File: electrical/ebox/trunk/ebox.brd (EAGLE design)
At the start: 127 x 101.6 mm, 161 parts, among them IC1 MAX3221CUE, IC10 SN74LVC1G125, IC11 MAX3221CUE, IC12 INA170, IC13 SN74LVC1G125, IC14 SN74LVC1G125, IC15 MAX3221CUE, IC16 MCP170333MB, IC17 SN74LVC1G125, IC18 SN74LVC1G125, IC19 74ALS04D, IC2 LT3652, IC3 XMEGA128A1, IC4 LT1161, IC5 SN74LVC1G125, IC6 SN74LVC1G125, IC7 MAX3221CUE, IC8 INA170, IC9 SN74LVC1G125, Q1 FDD4141TO252, U1 BLUETOOTH-RN42, U2 D2523T_, X1 7381-3PG-300, X10 DEANS-MALE, X11 B4B-ZR, X12 DEANS-MALE, X13 B4B-ZR, X14 22-23-2021, X15 DEANS-FEMALE, X16 DEANS-FEMALE, X17 USB_A, X18 22-23-2021, X2 7381-3PG-300, X3 7381-2PG-300, X4 17984-7PG-300, X5 17984-7PG-300, X6 17984-7PG-300, X7 17984-7PG-300, X8 22-23-2031, X9 22-23-2031

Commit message: Cleaned up more stuff.  Just need to do final check and silkscreen work.
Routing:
- net MOT1_C: track 30.6 -> 0.00 mm
- net MOT2_C: track 30.6 -> 0.00 mm
- net CHARGE: track 20.9 -> 0.00 mm
- net MOT2_A: track 20.0 -> 0.00 mm
- net MOT1_A: track 20.0 -> 0.00 mm
- net MOT2_B: track 18.5 -> 0.00 mm
- net MOT1_B: track 18.5 -> 0.00 mm
- net +3V3: track 424.1 -> 417.6 mm
- net BT_STATUS: track 64.8 -> 63.0 mm
- net N$19: track 60.2 -> 58.7 mm
- net N$7: track 28.9 -> 30.2 mm
- net N$14: track 60.2 -> 59.1 mm
- net N$20: track 80.5 -> 81.5 mm
- net N$16: track 97.5 -> 98.5 mm
- net N$15: track 74.5 -> 75.6 mm
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- added copper zone on layer 1, net CHARGE
- added copper zone on layer 1, net MOT1_A
- added copper zone on layer 1, net MOT1_B
- added copper zone on layer 1, net MOT1_C
- added copper zone on layer 1, net MOT2_A
- added copper zone on layer 1, net MOT2_B
- added copper zone on layer 1, net MOT2_C

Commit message: Updated some silkscreen on various areas.
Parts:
- moved X8 1.91 mm to (28.6, 5.08)
- moved X9 1.27 mm to (21.6, 5.08)
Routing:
- net MOT1_SIG: track 27.3 -> 29.2 mm
- net MOT1_5V: track 6.13 -> 8.04 mm
- net MOT2_5V: track 13.8 -> 15.0 mm
- net MOT2_SIG: track 35.4 -> 36.7 mm

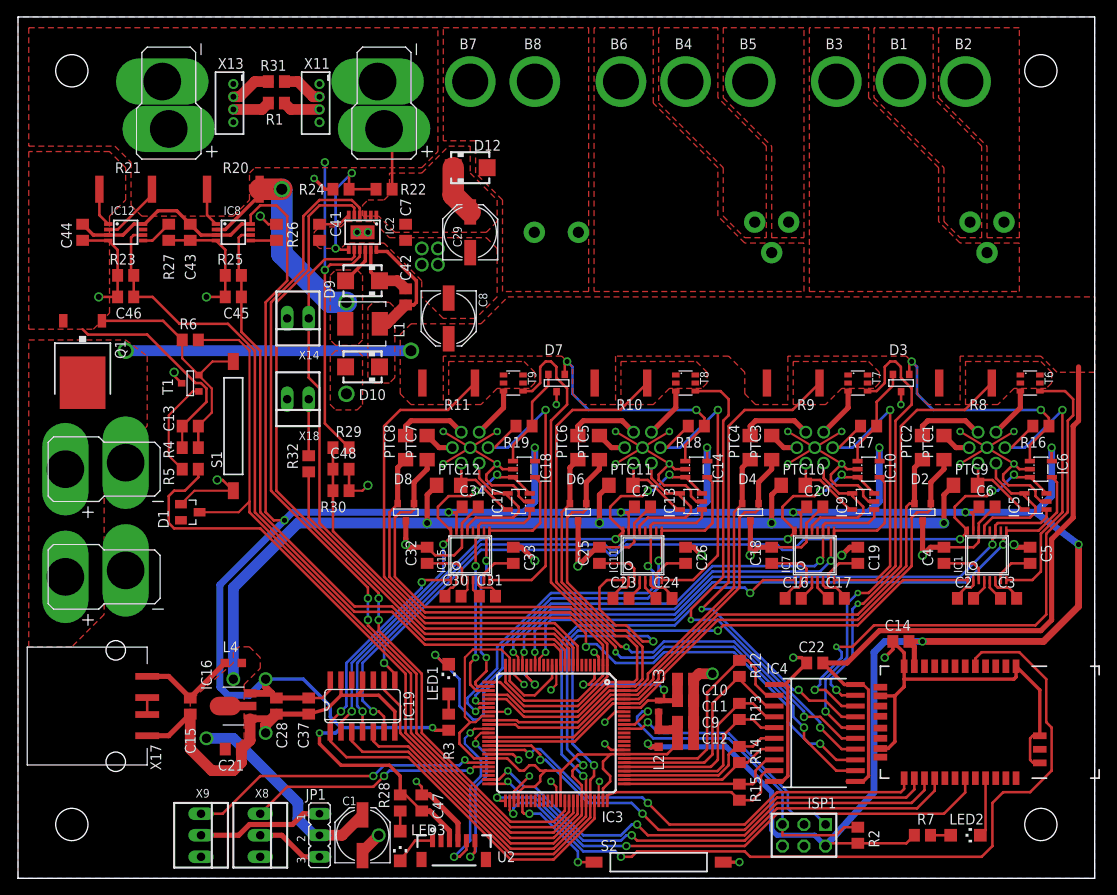
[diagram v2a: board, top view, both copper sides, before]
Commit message: Silkscreening complete.  Prepped for DFM check.
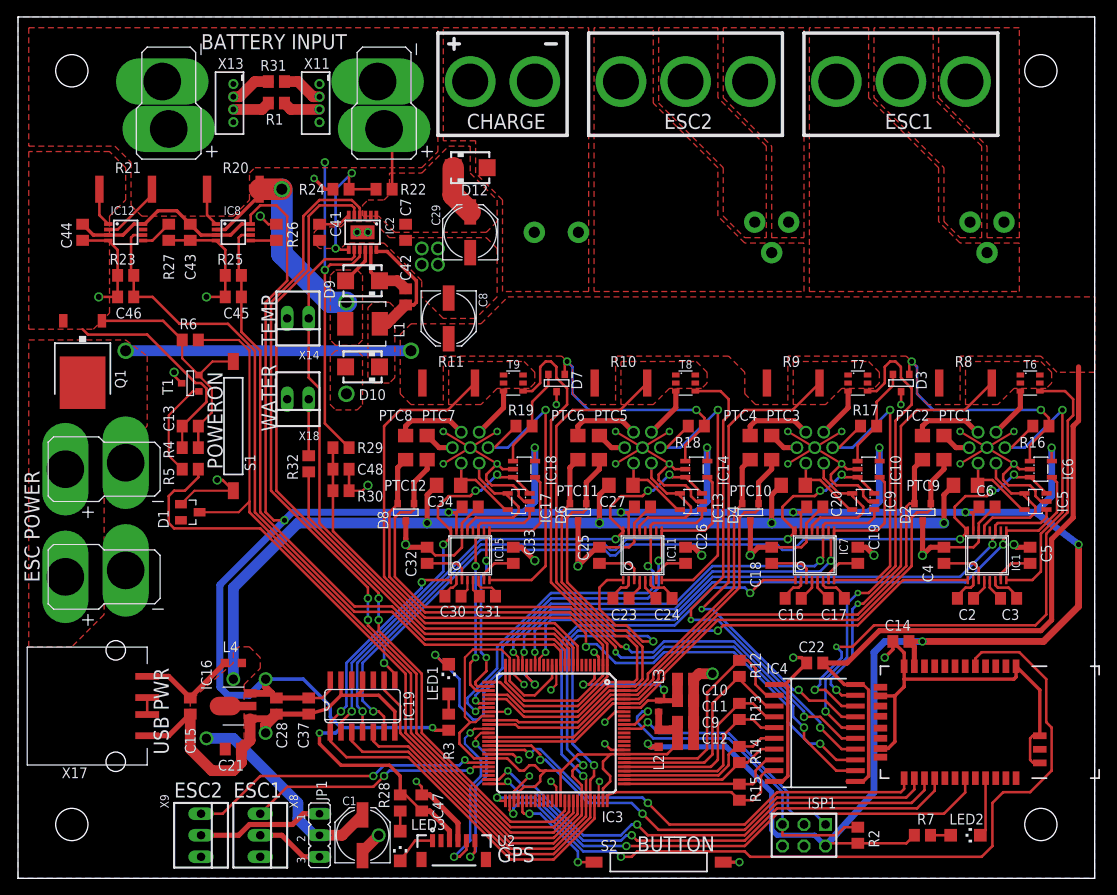
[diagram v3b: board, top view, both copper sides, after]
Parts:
- added U$1: PLATYPUS_LOGO, crw:PLATYPUS_LOGO_SMALL
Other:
- board text added: "BATTERY INPUT"
- board text added: "BUTTON"
- board text added: "CHARGE"
- board text added: "ESC POWER"
- board text added: "ESC1"
- board text added: "ESC2"
- board text added: "GPS"
- board text added: "Main Control Board"
- board text added: "PORT 1"
- board text added: "PORT 2"
- board text added: "PORT 3"
- board text added: "PORT 4"
- board text added: "POWERON"
- board text added: "Revision A, (C) 2012"
- board text added: "TEMP"
- board text added: "USB PWR"
- board text added: "WATER"
